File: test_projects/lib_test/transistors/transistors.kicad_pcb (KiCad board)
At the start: 2 copper layers, 78 x 17 mm, 9 parts, among them Q1001 BC850B, Q1002 BC860B, Q1003 BD139, Q1004 BD140, Q1005 MJL3281A, Q1006 MJL1302A, Q1007 MMBT2222AL, Q1008 DMG3406L, Q1009 DMP3028LFDE

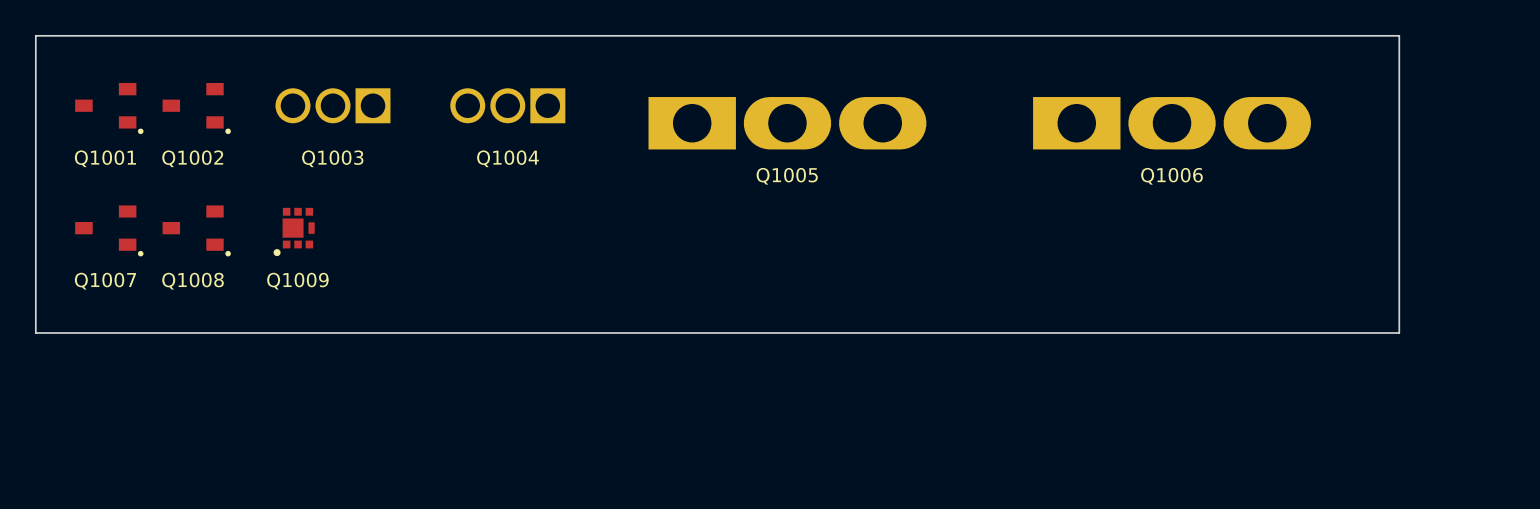
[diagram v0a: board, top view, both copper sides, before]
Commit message: add heatsink to test project
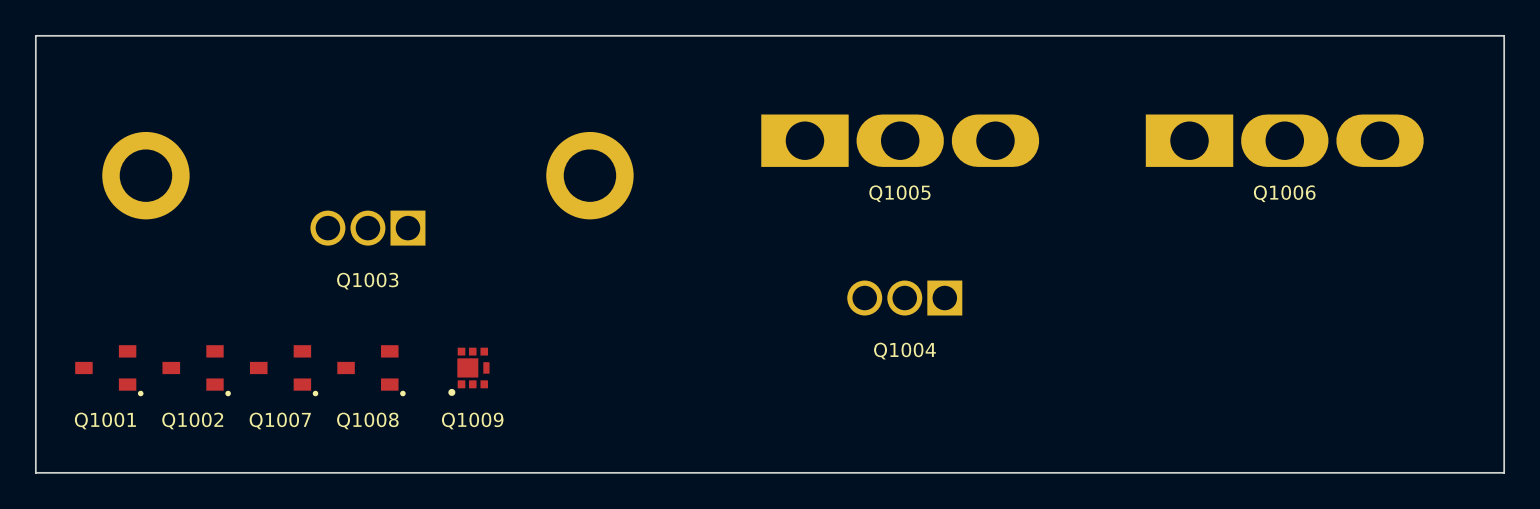
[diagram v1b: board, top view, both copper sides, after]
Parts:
- added M1: mec_heatsink_sk104_12.7x34.9x38.1mm, lily_footprints:mec_heatsink_sk104_12.7x34.9x38.1mm, F.Cu at (129.0, 78.0)
- moved Q1004 25.2 mm to (157.4, 85.0)
- moved Q1001 15.0 mm to (114.0, 89.0)
- moved Q1002 15.0 mm to (119.0, 89.0)
- moved Q1007 12.8 mm to (124.0, 89.0)
- moved Q1008 12.8 mm to (129.0, 89.0)
- moved Q1009 12.8 mm to (135.0, 89.0)
- moved Q1003 7.28 mm to (126.7, 81.0)
- moved Q1005 6.53 mm to (154.0, 76.0)
- moved Q1006 6.53 mm to (176.0, 76.0)
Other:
- board size 78 x 17 mm -> 84 x 25 mm
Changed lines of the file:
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@@
 	(footprint "lily_footprints:sot23"
 		(layer "F.Cu")
-		(at 114 74)
+		(at 114 89)
 		(property "Reference" "Q1001"
 			(at 0 3 180)
@@
 	(footprint "lily_footprints:sot23"
 		(layer "F.Cu")
-		(at 114 81)
+		(at 124 89)
 		(property "Reference" "Q1007"
 			(at 0 3 0)
@@
 	(footprint "lily_footprints:to264"
 		(layer "F.Cu")
-		(at 147.55 75)
+		(at 154 76)
 		(property "Reference" "Q1005"
 			(at 5.45 3 0)
@@
 	(footprint "lily_footprints:sot23"
 		(layer "F.Cu")
-		(at 119 81)
+		(at 129 89)
 		(property "Reference" "Q1008"
 			(at 0 3 0)
@@
 	(footprint "lily_footprints:sot1220_dnf2020md-6_type_e"
 		(layer "F.Cu")
-		(at 125 81)
+		(at 135 89)
 		(property "Reference" "Q1009"
 			(at 0 3 0)
@@
 	(footprint "lily_footprints:to126"
 		(layer "F.Cu")
-		(at 124.71 74)
+		(at 126.71 81)
 		(property "Reference" "Q1003"
 			(at 2.29 3 0)
@@
 	(footprint "lily_footprints:to264"
 		(layer "F.Cu")
-		(at 169.55 75)
+		(at 176 76)
 		(property "Reference" "Q1006"
 			(at 5.45 3 0)
@@
 		)
 	)
+	(footprint "lily_footprints:mec_heatsink_sk104_12.7x34.9x38.1mm"
+		(layer "F.Cu")
+		(at 129 78)
+		(property "Reference" "M1"
+			(at 0 0 0)
+			(layer "F.SilkS")
+			(hide yes)
+			(effects
+				(font
+					(size 0.8 0.8)
+					(thickness 0.16)
+				)
+			)
+		)
+		(property "Value" "mec_heatsink_sk104_12.7x34.9x38.1mm"
+			(at 0 0 0)
+			(layer "F.Fab")
+			(hide yes)
+			(effects
+				(font
+					(size 0.5 0.5)
+					(thickness 0.1)
+				)
+			)
+		)
+		(property "Datasheet" "https://lilytronics.github.io/lily_kicad_lib/datasheets/fisher/heatsink_SK_104_38,1_STC.pdf"
+			(at 0 0 0)
+			(unlocked yes)
+			(layer "F.Fab")
+			(hide yes)
+			(effects
+				(font
+					(size 1.27 1.27)
+					(thickness 0.15)
+				)
+			)
+		)
+		(property "Description" ""
+			(at 0 0 0)
+			(unlocked yes)
+			(layer "F.Fab")
+			(hide yes)
+			(effects
+				(font
+					(size 1.27 1.27)
+					(thickness 0.15)
+				)
+			)
+		)
+		(property "Revision" "1"
+			(at 0 0 0)
+			(unlocked yes)
+			(layer "F.Fab")
+			(hide yes)
+			(effects
+				(font
+					(size 0.5 0.5)
+					(thickness 0.1)
+				)
+			)
+		)
+		(property "Status" "Active"
+			(at 0 0 0)
+			(unlocked yes)
+			(layer "F.Fab")
+			(hide yes)
+			(effects
+				(font
+					(size 1 1)
+					(thickness 0.15)
+				)
+			)
+		)
+		(property "Manufacturer" "Fisher"
+			(at 0 0 0)
+			(unlocked yes)
+			(layer "F.Fab")
+			(hide yes)
+			(effects
+				(font
+					(size 1 1)
+					(thickness 0.15)
+				)
+			)
+		)
+		(property "Manufacturer_ID" "SK 104 38,1 STS"
+			(at 0 0 0)
+			(unlocked yes)
+			(layer "F.Fab")
+			(hide yes)
+			(effects
+				(font
+					(size 1 1)
+					(thickness 0.15)
+				)
+			)
+		)
+		(property "Lily_ID" "1718-10001"
+			(at 0 0 0)
+			(unlocked yes)
+			(layer "F.Fab")
+			(hide yes)
+			(effects
+				(font
+					(size 1 1)
+					(thickness 0.15)
+				)
+			)
+		)
+		(property "JLCPCB_ID" "NO_ID"
+			(at 0 0 0)
+			(unlocked yes)
+			(layer "F.Fab")
+			(hide yes)
+			(effects
+				(font
+					(size 1 1)
+					(thickness 0.15)
+				)
+			)
+		)
+		(sheetname "/")
+		(sheetfile "transistors.kicad_sch")
+		(units
+			(unit
+				(name "A")
+				(pins "1")
+			)
+		)
+		(attr through_hole exclude_from_pos_files)
+		(duplicate_pad_numbers_are_jumpers no)
+		(fp_poly
+			(pts
+				(xy -7.4 -6.9) (xy -7.4 -0.75) (xy 7.4 -0.75) (xy 7.4 -6.9) (xy 18 -6.9) (xy 18 6.9) (xy 7.4 6.9)
+				(xy 7.4 0.75) (xy -7.4 0.75) (xy -7.4 6.9) (xy -18 6.9) (xy -18 -6.9)
+			)
+			(stroke
+				(width 0.05)
+				(type solid)
+			)
+			(fill no)
+			(layer "F.CrtYd")
+		)
+		(fp_poly
+			(pts
+				(xy -7.95 -0.75) (xy 7.95 -0.75) (xy 7.95 -6.35) (xy 17.45 -6.35) (xy 17.45 6.35) (xy 7.95 6.35)
+				(xy 7.95 0.75) (xy -7.95 0.75) (xy -7.95 6.35) (xy -17.45 6.35) (xy -17.45 -6.35) (xy -7.95 -6.35)
+			)
+			(stroke
+				(width 0.1)
+				(type solid)
+			)
+			(fill no)
+			(layer "F.Fab")
+		)
+		(fp_text user "${REFERENCE}"
+			(at 0 0 0)
+			(layer "F.Fab")
+			(effects
+				(font
+					(size 0.5 0.5)
+					(thickness 0.1)
+				)
+			)
+		)
+		(pad "1" thru_hole circle
+			(at -12.7 0)
+			(size 5 5)
+			(drill 3)
+			(layers "*.Cu" "*.Mask")
+			(remove_unused_layers no)
+			(net "unconnected-(M1-Pad1)")
+			(pintype "no_connect")
+			(solder_mask_margin 0.05)
+			(solder_paste_margin -0.05)
+		)
+		(pad "1" thru_hole circle
+			(at 12.7 0)
+			(size 5 5)
+			(drill 3)
+			(layers "*.Cu" "*.Mask")
+			(remove_unused_layers no)
+			(net "unconnected-(M1-Pad1)_1")
+			(pintype "no_connect")
+			(solder_mask_margin 0.05)
+			(solder_paste_margin -0.05)
+		)
+		(embedded_fonts no)
+		(model "../3d_models/mec_heatsink_sk104_12.7x34.9x38.1mm.step"
+			(offset
+				(xyz 0 0 0)
+			)
+			(scale
+				(xyz 1 1 1)
+			)
+			(rotate
+				(xyz 0 0 0)
+			)
+		)
+	)
 	(footprint "lily_footprints:to126"
 		(layer "F.Cu")
-		(at 134.71 74)
+		(at 157.42 85)
 		(property "Reference" "Q1004"
 			(at 2.3 3 0)
@@
 	(footprint "lily_footprints:sot23"
 		(layer "F.Cu")
-		(at 119 74)
+		(at 119 89)
 		(property "Reference" "Q1002"
 			(at 0 3 0)
@@
 	(gr_rect
 		(start 110 70)
-		(end 188 87)
+		(end 194 95)
 		(stroke
 			(width 0.1)

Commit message: add triac
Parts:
- added Q1009: BTA206X-800CT, lily_footprints:to220f, F.Cu at (178.0, 85.2)
- renumbered M1 to M1001, Q1009 to Q1010
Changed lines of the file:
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@@
+		)
+	)
+	(footprint "lily_footprints:to220f"
+		(layer "F.Cu")
+		(at 178 85.225)
+		(property "Reference" "Q1009"
+			(at 2.54 2.775 0)
+			(layer "F.SilkS")
+			(effects
+				(font
+					(size 0.8 0.8)
+					(thickness 0.16)
+				)
+			)
+		)
+		(property "Value" "BTA206X-800CT"
+			(at 2.54 0 0)
+			(layer "F.Fab")
+			(hide yes)
+			(effects
+				(font
+					(size 0.5 0.5)
+					(thickness 0.1)
+				)
+			)
+		)
+		(property "Datasheet" "https://lilytronics.github.io/lily_kicad_lib/datasheets/ween/BTA206X-800CT.pdf"
+			(at 0 0 0)
+			(unlocked yes)
+			(layer "F.Fab")
+			(hide yes)
+			(effects
+				(font
+					(size 1.27 1.27)
+					(thickness 0.15)
+				)
+			)
+		)
+		(property "Description" ""
+			(at 0 0 0)
+			(unlocked yes)
+			(layer "F.Fab")
+			(hide yes)
+			(effects
+				(font
+					(size 1.27 1.27)
+					(thickness 0.15)
+				)
+			)
+		)
+		(property "Revision" "1"
+			(at 0 0 0)
+			(unlocked yes)
+			(layer "F.Fab")
+			(hide yes)
+			(effects
+				(font
+					(size 0.5 0.5)
+					(thickness 0.1)
+				)
+			)
+		)
+		(property "Status" "Active"
+			(at 0 0 0)
+			(unlocked yes)
+			(layer "F.Fab")
+			(hide yes)
+			(effects
+				(font
+					(size 1 1)
+					(thickness 0.15)
+				)
+			)
+		)
+		(property "Manufacturer" "WeEn"
+			(at 0 0 0)
+			(unlocked yes)
+			(layer "F.Fab")
+			(hide yes)
+			(effects
+				(font
+					(size 1 1)
+					(thickness 0.15)
+				)
+			)
+		)
+		(property "Manufacturer_ID" "BTA206X-800CT"
+			(at 0 0 0)
+			(unlocked yes)
+			(layer "F.Fab")
+			(hide yes)
+			(effects
+				(font
+					(size 1 1)
+					(thickness 0.15)
+				)
+			)
+		)
+		(property "Lily_ID" "1918-10010"
+			(at 0 0 0)
+			(unlocked yes)
+			(layer "F.Fab")
+			(hide yes)
+			(effects
+				(font
+					(size 1 1)
+					(thickness 0.15)
+				)
+			)
+		)
+		(property "JLCPCB_ID" "NO_ID"
+			(at 0 0 0)
+			(unlocked yes)
+			(layer "F.Fab")
+			(hide yes)
+			(effects
+				(font
+					(size 1 1)
+					(thickness 0.15)
+				)
+			)
+		)
+		(sheetname "/")
+		(sheetfile "transistors.kicad_sch")
+		(units
+			(unit
+				(name "A")
+				(pins "3" "2" "1")
+			)
+		)
+		(attr through_hole exclude_from_pos_files)
+		(duplicate_pad_numbers_are_jumpers no)
+		(fp_rect
+			(start -2.61 -3.25)
+			(end 7.69 1.35)
+			(stroke
+				(width 0.1)
+				(type solid)
+			)
+			(fill no)
+			(layer "F.SilkS")
+		)
+		(fp_rect
+			(start -2.91 -3.5)
+			(end 7.99 1.6)
+			(stroke
+				(width 0.05)
+				(type solid)
+			)
+			(fill no)
+			(layer "F.CrtYd")
+		)
+		(fp_text user "${REFERENCE}"
+			(at 2.54 -2.3 0)
+			(layer "F.Fab")
+			(effects
+				(font
+					(size 0.5 0.5)
+					(thickness 0.1)
+					(bold yes)
+				)
+			)
+		)
+		(pad "1" thru_hole rect
+			(at 0 0)
+			(size 2.2 2.2)
+			(drill 1.2)
+			(layers "*.Cu" "*.Mask")
+			(remove_unused_layers no)
+			(net "unconnected-(Q1009-Pad1)")
+			(pintype "passive")
+			(solder_mask_margin 0.1)
+		)
+		(pad "2" thru_hole circle
+			(at 2.54 0)
+			(size 2.2 2.2)
+			(drill 1.2)
+			(layers "*.Cu" "*.Mask")
+			(remove_unused_layers no)
+			(net "unconnected-(Q1009-Pad2)")
+			(pintype "passive")
+			(solder_mask_margin 0.1)
+		)
+		(pad "3" thru_hole circle
+			(at 5.08 0)
+			(size 2.2 2.2)
+			(drill 1.2)
+			(layers "*.Cu" "*.Mask")
+			(remove_unused_layers no)
+			(net "unconnected-(Q1009-Pad3)")
+			(pintype "passive")
+			(solder_mask_margin 0.1)
+		)
+		(embedded_fonts no)
+		(model "../3d_models/to220f.step"
+			(offset
+				(xyz 0 0 1)
+			)
+			(scale
+				(xyz 1 1 1)
+			)
+			(rotate
+				(xyz -0 -0 -0)
+			)
 		)
 	)
@@
 		(layer "F.Cu")
 		(at 135 89)
-		(property "Reference" "Q1009"
+		(property "Reference" "Q1010"
 			(at 0 3 0)
 			(unlocked yes)
@@
 			(size 0.45 0.43)
 			(layers "F.Cu" "F.Mask" "F.Paste")
-			(net "unconnected-(Q1009-Pad1)")
+			(net "unconnected-(Q1010-Pad1)")
 			(pintype "passive")
 			(solder_mask_margin 0.15)
@@
 			(size 0.45 0.43)
 			(layers "F.Cu" "F.Mask" "F.Paste")
-			(net "unconnected-(Q1009-Pad2)")
+			(net "unconnected-(Q1010-Pad2)")
 			(pintype "passive")
 			(solder_mask_margin 0.15)
@@
 			(size 0.45 0.43)
 			(layers "F.Cu" "F.Mask" "F.Paste")
-			(net "unconnected-(Q1009-Pad3)")
+			(net "unconnected-(Q1010-Pad3)")
 			(pintype "passive")
 			(solder_mask_margin 0.15)
@@
 			(size 0.45 0.43)
 			(layers "F.Cu" "F.Mask" "F.Paste")
-			(net "unconnected-(Q1009-Pad4)")
+			(net "unconnected-(Q1010-Pad4)")
 			(pintype "passive")
 			(solder_mask_margin 0.15)
@@
 			(size 0.45 0.43)
 			(layers "F.Cu" "F.Mask" "F.Paste")
-			(net "unconnected-(Q1009-Pad5)")
+			(net "unconnected-(Q1010-Pad5)")
 			(pintype "passive")
 			(solder_mask_margin 0.15)
@@
 			(size 0.45 0.43)
 			(layers "F.Cu" "F.Mask" "F.Paste")
-			(net "unconnected-(Q1009-Pad6)")
+			(net "unconnected-(Q1010-Pad6)")
 			(pintype "passive")
 			(solder_mask_margin 0.15)
@@
 			(size 1.1 1.2)
 			(layers "F.Cu" "F.Mask" "F.Paste")
-			(net "unconnected-(Q1009-Pad7)")
+			(net "unconnected-(Q1010-Pad7)")
 			(pintype "passive")
 			(solder_mask_margin 0.1)
@@
 			(size 0.66 0.35)
 			(layers "F.Cu" "F.Mask" "F.Paste")
-			(net "unconnected-(Q1009-Pad8)")
+			(net "unconnected-(Q1010-Pad8)")
 			(pintype "passive")
 			(solder_mask_margin 0.1)
@@
 		(layer "F.Cu")
 		(at 129 78)
-		(property "Reference" "M1"
+		(property "Reference" "M1001"
 			(at 0 0 0)
 			(layer "F.SilkS")
@@
 			(layers "*.Cu" "*.Mask")
 			(remove_unused_layers no)
-			(net "unconnected-(M1-Pad1)")
+			(net "unconnected-(M1001-Pad1)")
 			(pintype "no_connect")
 			(solder_mask_margin 0.05)
@@
 			(layers "*.Cu" "*.Mask")
 			(remove_unused_layers no)
-			(net "unconnected-(M1-Pad1)_1")
+			(net "unconnected-(M1001-Pad1)_1")
 			(pintype "no_connect")
 			(solder_mask_margin 0.05)
